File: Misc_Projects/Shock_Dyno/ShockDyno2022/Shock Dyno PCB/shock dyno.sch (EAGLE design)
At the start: 30 parts, among them IC1 ADS8332IBPWR, J1 1985195, K1 T9GS1L14-5, U1 REF5040AIDR

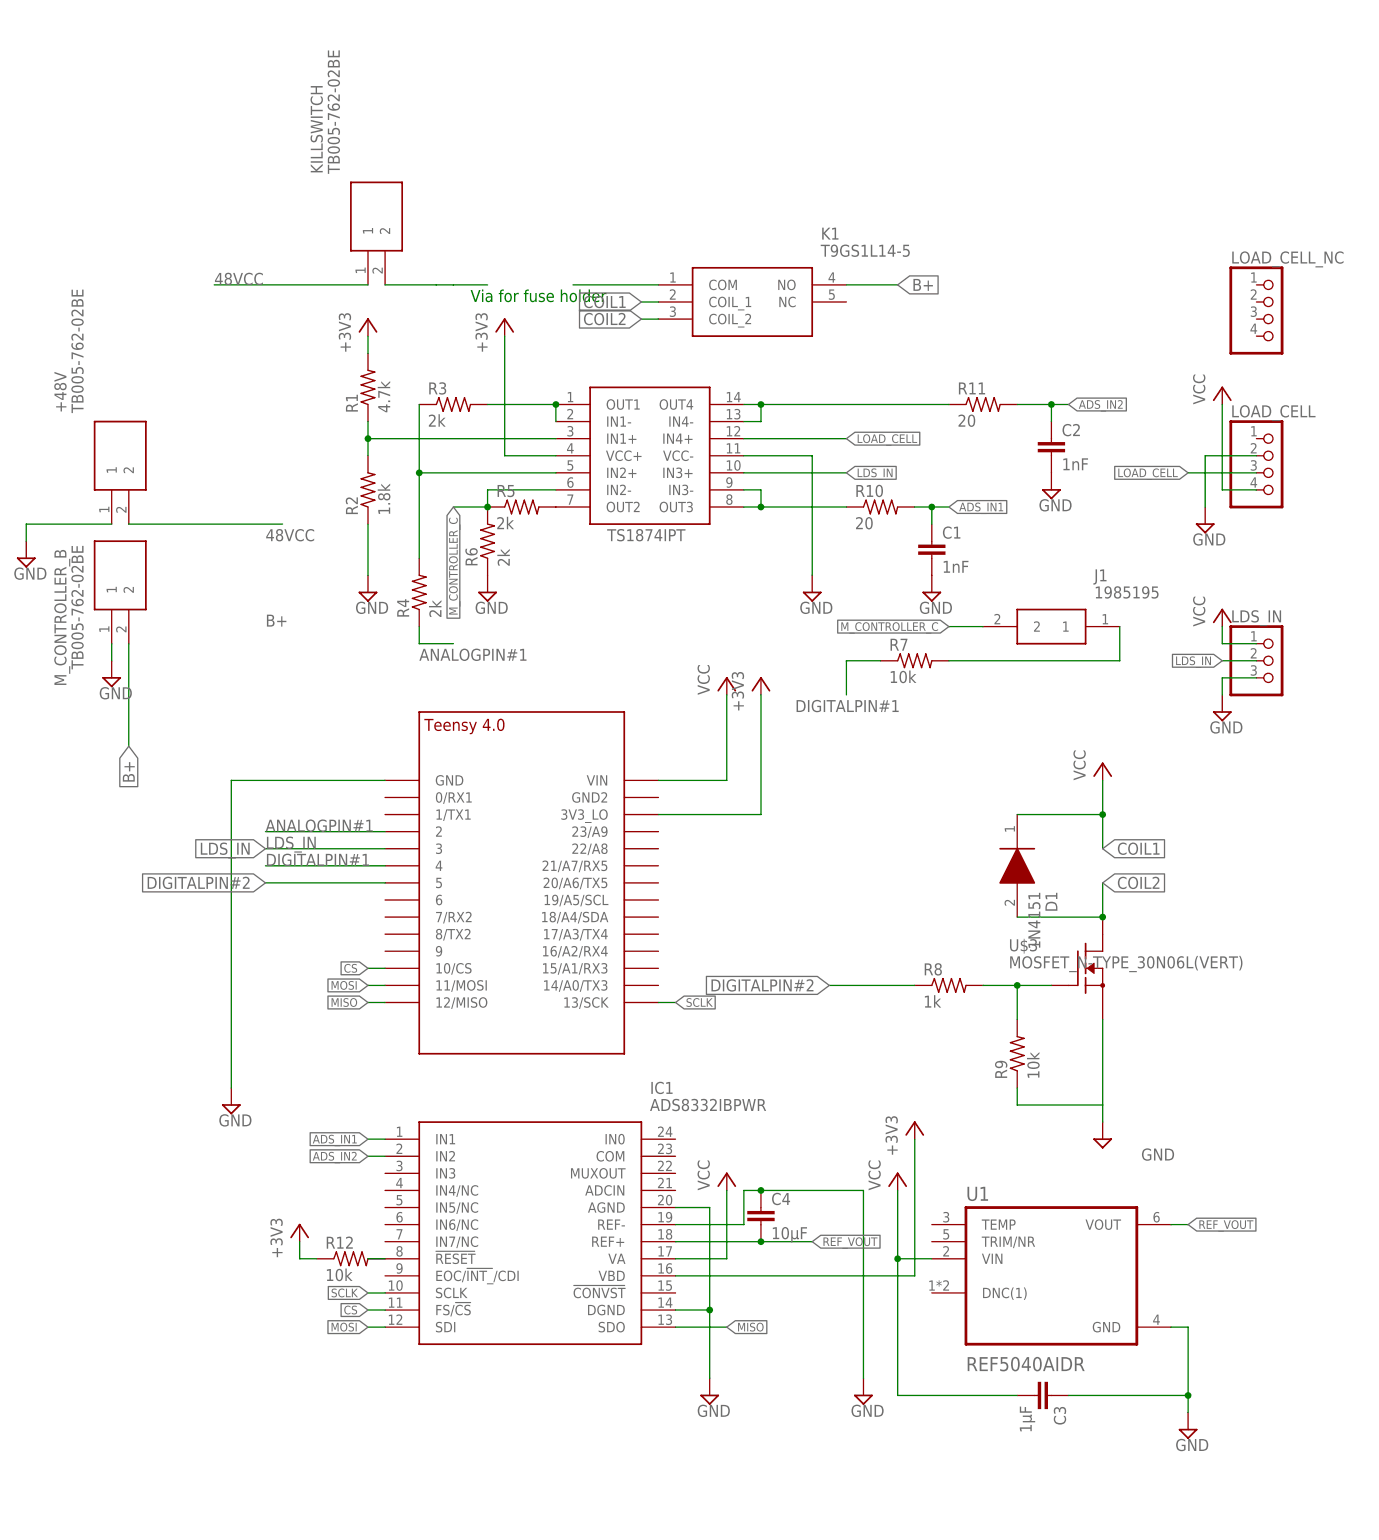
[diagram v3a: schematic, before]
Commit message: shock dyno PCB updates
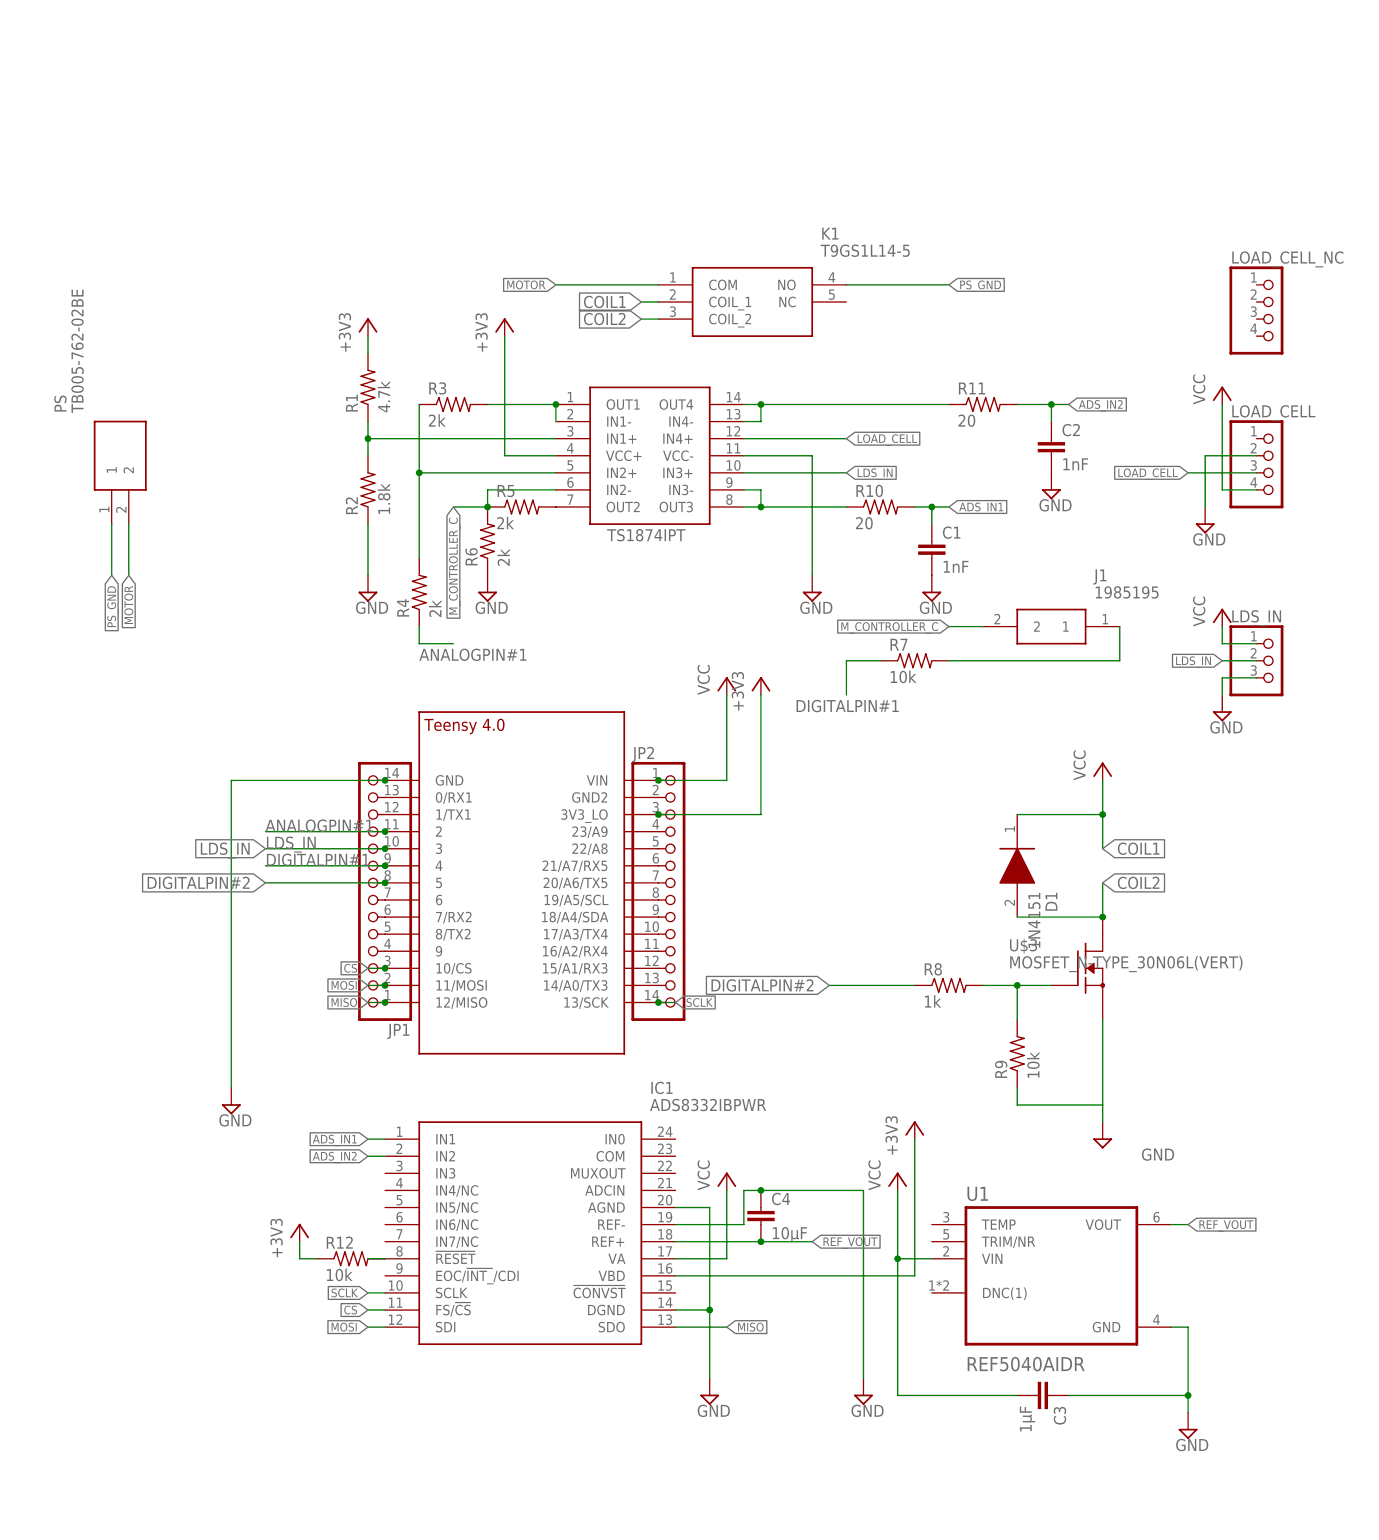
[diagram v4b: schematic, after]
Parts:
- removed KILLSWITCH, M_CONTROLLER_B: TB005-762-02BE, GTOR - Connectors:TB005-762-02BE
- added JP1, JP2: (no value), GTOR - Connectors:PINHD-1X14
- renumbered +48V to PS
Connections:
- removed net 48VCC: KILLSWITCH.1, PS.2
- removed net B+: K1.NO, M_CONTROLLER_B.2
- new net MOTOR: K1.COM, PS.2
- new net N$13: JP1.7, U$2.6
- new net N$14: JP1.12, U$2.1/TX1
- new net N$15: JP1.13, U$2.0/RX1
- new net N$16: JP2.2, U$2.GND2
- new net N$17: JP2.4, U$2.23/A9
- new net N$18: JP2.5, U$2.22/A8
- new net N$19: JP2.6, U$2.21/A7/RX5
- new net N$20: JP2.7, U$2.20/A6/TX5
- new net N$21: JP2.8, U$2.19/A5/SCL
- new net N$22: JP2.9, U$2.18/A4/SDA
- new net N$23: JP2.10, U$2.17/A3/TX4
- new net N$24: JP2.11, U$2.16/A2/RX4
- new net N$25: JP2.12, U$2.15/A1/RX3
- new net N$26: JP2.13, U$2.14/A0/TX3
- new net N$5: JP1.4, U$2.9
- new net PS_GND: K1.NO, PS.1
- net +3V3: now also JP2.3
- net ANALOGPIN#1: now also JP1.11
- net CS: now also JP1.3
- net DIGITALPIN#1: now also JP1.9
- net DIGITALPIN#2: now also JP1.8
- net GND: now also JP1.14; no longer M_CONTROLLER_B.1, PS.1
- net LDS_IN: now also JP1.10
- net MISO: now also JP1.1
- net MOSI: now also JP1.2
- net N$6: now also JP1.5, U$2.8/TX2; no longer KILLSWITCH.2
- net N$8: now also JP1.6, U$2.7/RX2; no longer K1.COM
- net SCLK: now also JP2.14
- net VCC: now also JP2.1
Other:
- note removed: "Via for fuse holder"

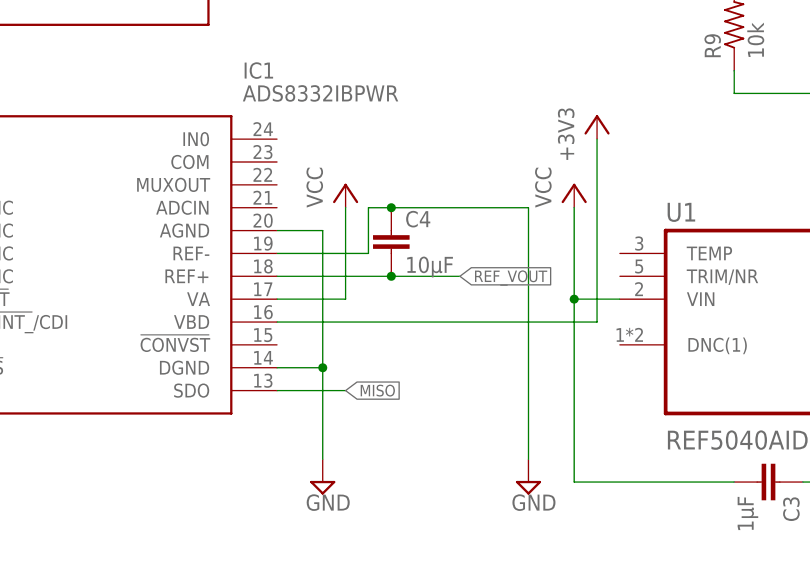
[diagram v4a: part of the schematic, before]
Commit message: update to shock dyno PCB design
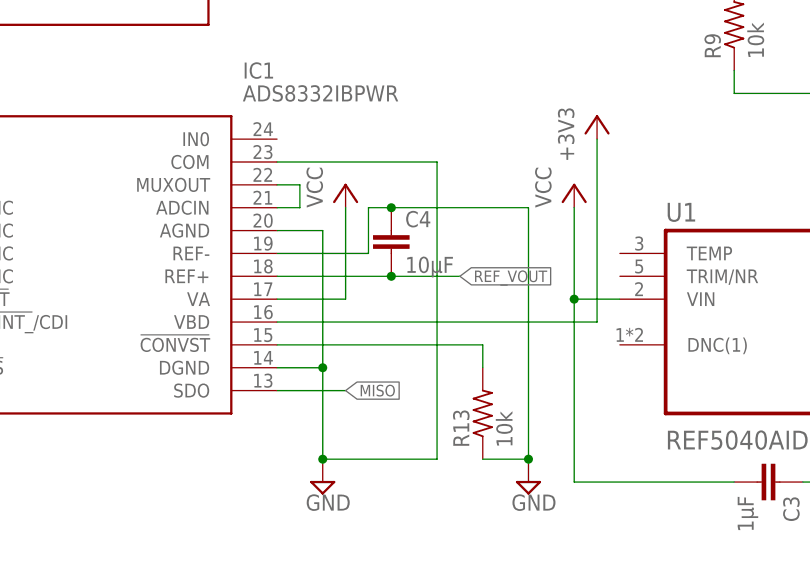
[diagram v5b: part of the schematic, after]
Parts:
- added R13: 10k, GTOR - Passive Components:RES_SMDR0603
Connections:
- new net N$27: IC1.!CONVST, R13.2
- new net N$28: IC1.ADCIN, IC1.MUXOUT
- net GND: now also IC1.COM, R13.1
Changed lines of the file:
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@@
 <part name="JP1" library="GTOR - Connectors" deviceset="PINHD-1X14" device="" package3d_urn="urn:adsk.eagle:package:22417/2"/>
 <part name="JP2" library="GTOR - Connectors" deviceset="PINHD-1X14" device="" package3d_urn="urn:adsk.eagle:package:22417/2"/>
+<part name="R13" library="GTOR - Passive Components" deviceset="RES_SMD" device="R0603" package3d_urn="urn:adsk.eagle:package:23555/3" value="10k"/>
 </parts>
 <sheets>
@@
 <attribute name="VALUE" x="34.29" y="-27.94" size="1.778" layer="96"/>
 </instance>
+<instance part="R13" gate="G$1" x="63.5" y="-73.66" smashed="yes" rot="R90">
+<attribute name="NAME" x="62.0014" y="-77.47" size="1.778" layer="95" rot="R90"/>
+<attribute name="VALUE" x="66.802" y="-77.47" size="1.778" layer="96" rot="R90"/>
+</instance>
 </instances>
 <busses>
@@
 <wire x1="45.72" y1="-68.58" x2="45.72" y2="-78.74" width="0.1524" layer="91"/>
 <junction x="45.72" y="-68.58"/>
+<pinref part="IC1" gate="G$1" pin="COM"/>
+<wire x1="40.64" y1="-45.72" x2="58.42" y2="-45.72" width="0.1524" layer="91"/>
+<wire x1="58.42" y1="-45.72" x2="58.42" y2="-78.74" width="0.1524" layer="91"/>
+<wire x1="58.42" y1="-78.74" x2="45.72" y2="-78.74" width="0.1524" layer="91"/>
+<junction x="45.72" y="-78.74"/>
 </segment>
 <segment>
@@
 <wire x1="68.58" y1="-50.8" x2="68.58" y2="-78.74" width="0.1524" layer="91"/>
 <pinref part="SUPPLY14" gate="GND" pin="GND"/>
+<pinref part="R13" gate="G$1" pin="1"/>
+<wire x1="63.5" y1="-78.74" x2="68.58" y2="-78.74" width="0.1524" layer="91"/>
+<junction x="68.58" y="-78.74"/>
 </segment>
 <segment>
@@
 </segment>
 </net>
+<net name="N$28" class="0">
+<segment>
+<pinref part="IC1" gate="G$1" pin="MUXOUT"/>
+<wire x1="40.64" y1="-48.26" x2="43.18" y2="-48.26" width="0.1524" layer="91"/>
+<wire x1="43.18" y1="-48.26" x2="43.18" y2="-50.8" width="0.1524" layer="91"/>
+<pinref part="IC1" gate="G$1" pin="ADCIN"/>
+<wire x1="43.18" y1="-50.8" x2="40.64" y2="-50.8" width="0.1524" layer="91"/>
+</segment>
+</net>
+<net name="N$27" class="0">
+<segment>
+<pinref part="IC1" gate="G$1" pin="!CONVST"/>
+<wire x1="40.64" y1="-66.04" x2="63.5" y2="-66.04" width="0.1524" layer="91"/>
+<pinref part="R13" gate="G$1" pin="2"/>
+<wire x1="63.5" y1="-66.04" x2="63.5" y2="-68.58" width="0.1524" layer="91"/>
+</segment>
+</net>
